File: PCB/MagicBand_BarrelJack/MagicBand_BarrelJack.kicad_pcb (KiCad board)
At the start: 2 copper layers, 40 x 40 mm, 22 parts, among them J2 PinSocket_1x08_P2.54mm_Vertic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, J3 PinHeader_1x03_P2.54mm_Vertic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, J6 JST_PH_B3B-PH-K_1x03_P2.00mm_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, J8 PinHeader_1x02_P2.54mm_Vertic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, J9 PinHeader_2x03_P2.54mm_Vertic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, Q1 SOT-23, U1 DIP-28_W7.62mm, U2 SOT-23, Y1 Crystal_HC49-4H_Vertical

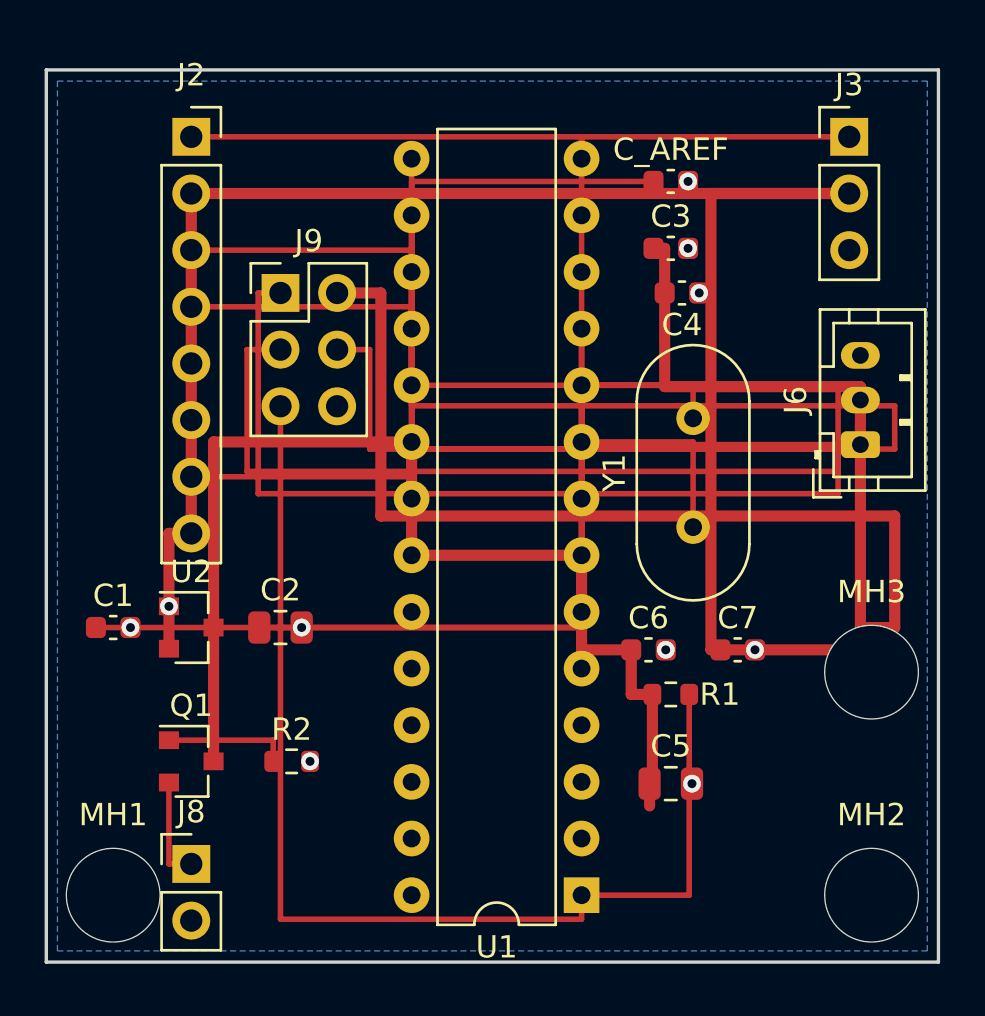
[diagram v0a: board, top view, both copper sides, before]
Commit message: Placement cleanup: reposition J8, fix U2/J2 silkscreen, remove J3 antenna keepout
Ripped up leftover tracks/vias from the earlier unsaved routing attempt and
refilled copper zones. DRC violations 176 -> 4 (remaining are cosmetic:
MH1 silk-edge clip, 3 pre-existing footprint-library path warnings).
42 unconnected pads is expected -- board has no routing yet.

Deleted J3's antenna keepout zone so FreeRouting can place vias/tracks near
it; will keep other copper off the antenna's near-field manually instead.
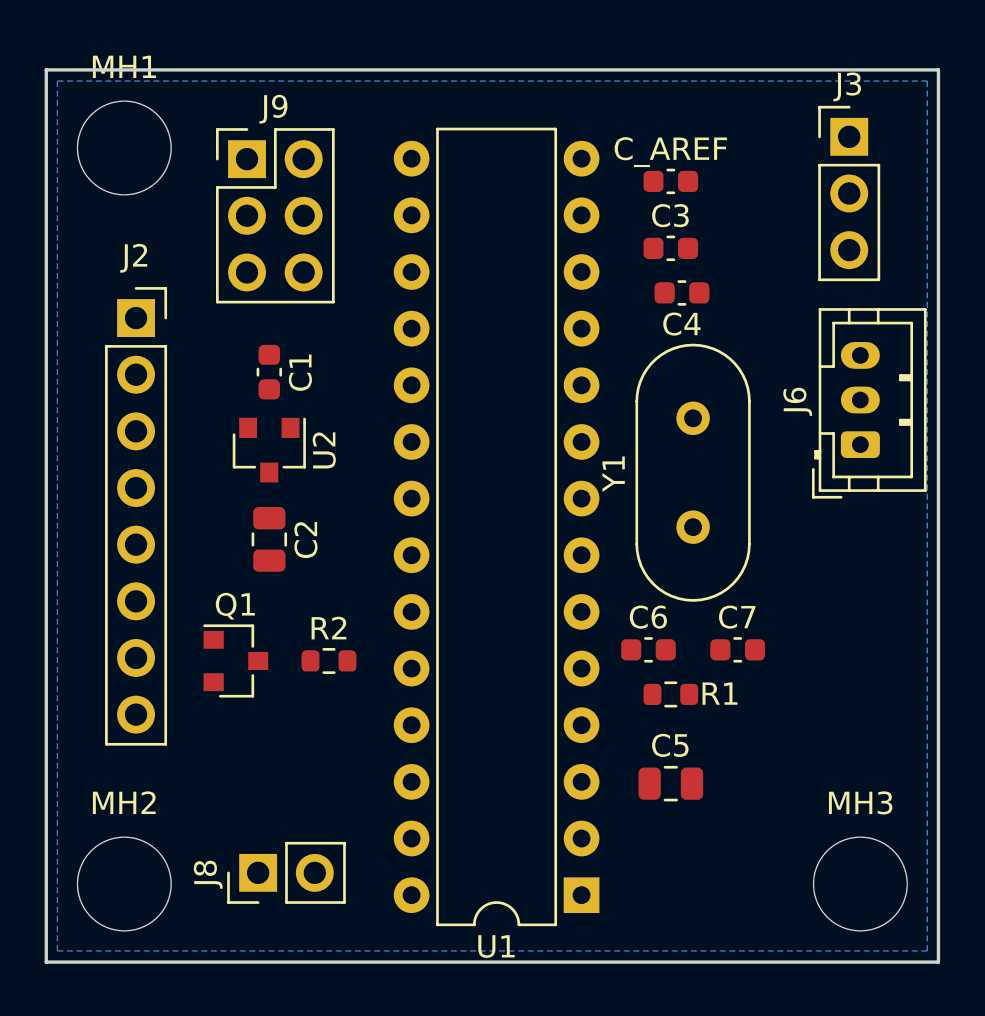
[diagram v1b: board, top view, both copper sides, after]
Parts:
- moved MH1 33.5 mm to (3.50, 3.50)
- moved MH2 33.5 mm to (3.50, 36.5)
- moved C1 13.4 mm to (10.0, 13.6), turned to -90 degrees
- moved MH3 9.51 mm to (36.5, 36.5)
- moved U2 8.69 mm to (10.0, 17.1), turned to -90 degrees
- moved J2 8.49 mm to (4.03, 11.1)
- moved J9 6.18 mm to (9.00, 4.00)
- moved Q1 4.92 mm to (8.50, 26.5)
- moved R2 4.80 mm to (12.7, 26.5)
- moved C2 3.98 mm to (10.0, 21.1), turned to -90 degrees
- moved J8 3.03 mm to (9.50, 36.0), turned to 90 degrees
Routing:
- net +5V: track 118.3 -> 0.00 mm
- net +3V3: track 83.8 -> 0.00 mm
- net D13: track 74.9 -> 0.00 mm
- net D12: track 73.4 -> 0.00 mm
- net D11: track 69.9 -> 0.00 mm
- net MCU_RESET: track 51.4 -> 0.00 mm
- net Net-(U1-XTAL1/PB6): track 38.9 -> 0.00 mm
- net D4: track 38.8 -> 0.00 mm
- net Net-(U1-XTAL2/PB7): track 31.8 -> 0.00 mm
- net Net-(U1-AREF): track 25.1 -> 0.00 mm
- net D9: track 24.1 -> 0.00 mm
- net D5: track 17.7 -> 0.00 mm
- net D8: track 13.0 -> 0.00 mm
- net Net-(Q1-Pin_1): track 5.62 -> 0.00 mm
- net Net-(J8-Pin_1): track 4.65 -> 0.00 mm
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
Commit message: FreeRouting pass: board fully routed, 0 unconnected nets
Exported Specctra DSN (GUI), ran FreeRouting headlessly (jar + JDK 25 JRE,
-de/-do/-mp 50), imported the resulting .ses back in KiCad, refilled zones.

DRC: 4 -> 52 (mid-import, stale zone fill) -> 8 after refill. Remaining 8:
4 pre-existing cosmetic (MH1 silk-edge clip, 3 footprint-library path
warnings) + 4 real starved-thermal/GND-pour bonding issues at J9 pad 6,
U1 pads 8 and 22, J2 pad 6 -- left for a follow-up GUI session.
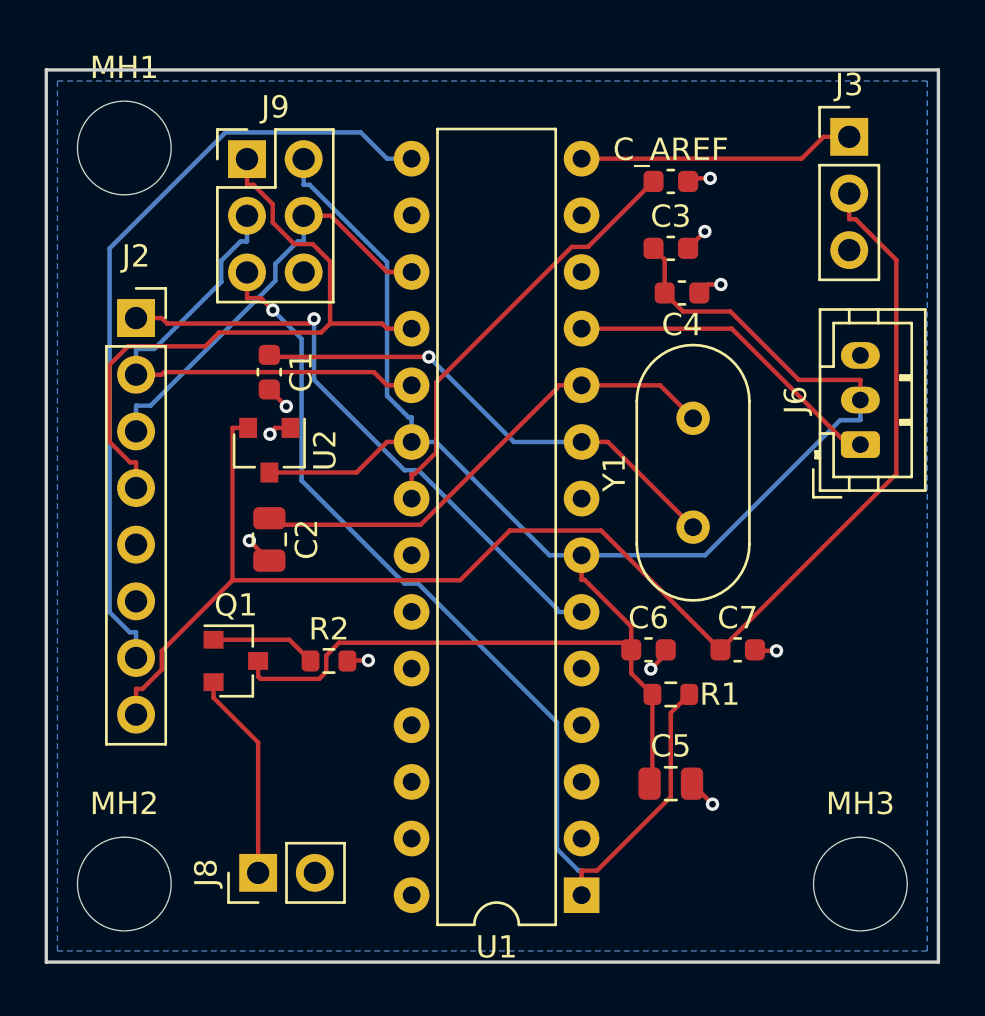
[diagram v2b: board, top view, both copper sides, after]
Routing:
- net +5V: track 0.00 -> 91.4 mm
- net +3V3: track 0.00 -> 65.3 mm
- net MCU_RESET: track 0.00 -> 46.3 mm, vias 0 -> 1
- net D9: track 0.00 -> 35.2 mm
- net D12: track 0.00 -> 30.2 mm
- net D4: track 0.00 -> 27.3 mm, vias 0 -> 1
- net D13: track 0.00 -> 22.5 mm
- net Net-(U1-XTAL2/PB7): track 0.00 -> 22.4 mm
- net Net-(U1-XTAL1/PB6): track 0.00 -> 22.2 mm, vias 0 -> 1
- net Net-(U1-AREF): track 0.00 -> 19.2 mm
- net D11: track 0.00 -> 19.2 mm
- net D5: track 0.00 -> 14.7 mm
- net D8: track 0.00 -> 12.4 mm
- net GND: track 0.00 -> 11.0 mm, vias 0 -> 10
- net Net-(J8-Pin_1): track 0.00 -> 9.38 mm
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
